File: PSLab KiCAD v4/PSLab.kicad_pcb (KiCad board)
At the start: 4 copper layers, 101.6 x 53.3 mm, 142 parts, among them CON1 USB-MICRO-B, J1 Programmer, J12 Sensors, J2 SQRs, J3 LA, J4 OSC_Pins, J5 Sin, J6 I2C, J7 IDs, J8 TX_RX_ES, J9 Test_Vs, P1 Power_Sources, P7 NRF, Q1 MMBT3906, Q2 MMBT3904, Q3 MMBT3906, U1 MCP2200, U10 TL082, U11 6S21, U12 6S21, U13 TL082, U15 ESP8266, U16 TL082, U2 74HC126, U3 PIC24EP256GP204, U4 TC1240A, U5 7660, U6 LM1117-3.3, U7 LM324, U8 TL082, U9 MCP4728, X1 12MHz

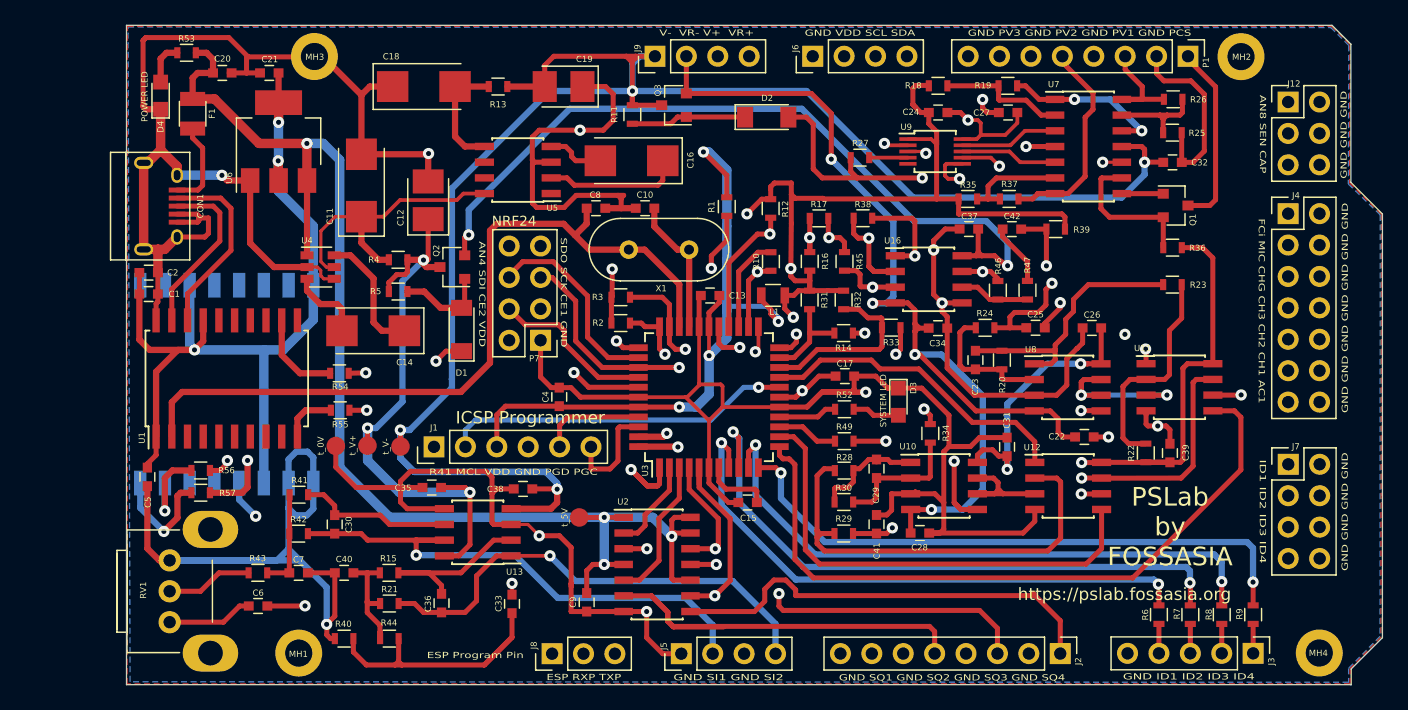
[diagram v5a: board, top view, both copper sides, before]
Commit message: Added guard rings for OSC
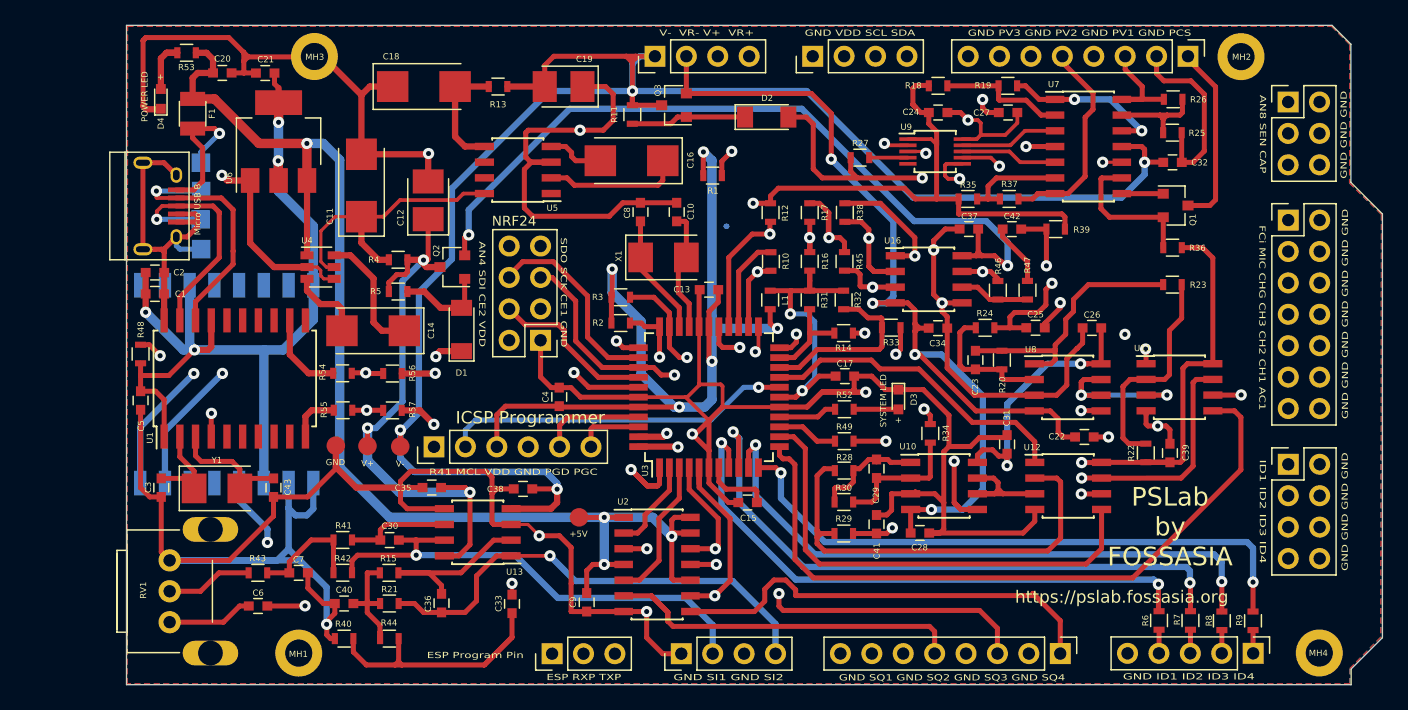
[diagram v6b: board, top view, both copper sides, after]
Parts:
- removed t_0V, t_5V, t_V+, t_V-: TEST, Measurement_Points:Measurement_Point_Round-SMD-Pad_Small
- added C3: 22p, Capacitors_SMD:C_0603, F.Cu at (93.8, 97.6)
- added C43: 22p, Capacitors_SMD:C_0603, F.Cu at (102.8, 97.6)
- added J10: GND, Measurement_Points:Measurement_Point_Square-SMD-Pad_Small, B.Cu at (97.0, 78.3)
- added J11: Vbus, Measurement_Points:Measurement_Point_Square-SMD-Pad_Small, B.Cu at (97.0, 71.4)
- added J13: D+, Measurement_Points:Measurement_Point_Square-SMD-Pad_Small, B.Cu at (97.0, 75.9)
- added J14: D-, Measurement_Points:Measurement_Point_Square-SMD-Pad_Small, B.Cu at (97.0, 73.7)
- added R48: 4.7k, Resistors_SMD:R_0603, F.Cu at (92.1, 86.8)
- added TP1: TEST, Measurement_Points:Measurement_Point_Round-SMD-Pad_Small, F.Cu at (113.1, 94.3)
- added TP2: TEST, Measurement_Points:Measurement_Point_Round-SMD-Pad_Small, F.Cu at (110.4, 94.3)
- added TP3: TEST, Measurement_Points:Measurement_Point_Round-SMD-Pad_Small, F.Cu at (127.5, 100.0)
- added TP4: TEST, Measurement_Points:Measurement_Point_Round-SMD-Pad_Small, F.Cu at (107.9, 94.2)
- added Y1: 12MHz, Crystals:Crystal_SMD_5032-2pin_5.0x3.2mm, F.Cu at (98.3, 97.7)
- CON1: value USB-MICRO-B -> USB-MINI-B
- D3, D4: footprint LEDs:LED_0805 -> LEDs:LED_0603
- L1: footprint Inductors_SMD:L_0805 -> Inductors_SMD:L_0603
- X1: value 12MHz -> 8MHz; footprint Crystals:Crystal_HC49-U_Vertical -> Crystals:Crystal_SMD_5032-2pin_5.0x3.2mm
- moved R56 17.4 mm to (112.5, 88.4), turned to 180 degrees
- moved R57 16.9 mm to (112.5, 91.4), turned to 180 degrees
- moved C5 6.20 mm to (92.1, 90.6)
- moved R41 5.10 mm to (108.4, 101.9)
- moved R42 4.77 mm to (108.4, 104.5)
- moved C30 4.62 mm to (112.2, 101.9), turned to 180 degrees
- moved C8 3.61 mm to (132.5, 75.3), turned to 270 degrees
- moved X1 2.88 mm to (134.4, 79.0)
- moved R1 2.76 mm to (138.3, 72.4), turned to 0 degrees
- moved C10 2.58 mm to (135.4, 75.3), turned to 270 degrees
- moved C40 2.48 mm to (108.5, 107.0)
- moved R38 1.53 mm to (149.1, 75.4), turned to 90 degrees
- moved R17 0.89 mm to (146.2, 75.4), turned to 90 degrees
- moved U1 0.65 mm to (99.7, 88.8)
- moved J4 0.52 mm to (184.9, 76.0)
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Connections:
- C8 pad 2: 12MHz -> Net-(C8-Pad2)
- U1 pad 2: 12MHz -> OS1
- U1 pad 3: (no net) -> OS2
- U1 pad 4: (no net) -> Net-(R48-Pad2)
- U3 pad 31: 12MHz -> Net-(C8-Pad2)
- X1 pad 1: 12MHz -> Net-(C8-Pad2)
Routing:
- net 12MHz: track 68.6 -> 0.00 mm
- net /RxD: track 153.9 -> 94.4 mm, vias 3 -> 2
- net /TxD: track 124.1 -> 73.6 mm, vias 3 -> 2
- net V-: track 193.7 -> 157.3 mm
- net Vdd: track 238.4 -> 210.2 mm, vias 8 -> 9
- net /ETxD: track 12.0 -> 34.8 mm, vias 1 -> 2
- net /ERxD: track 10.4 -> 32.1 mm, vias 1 -> 2
- net AVdd: track 175.8 -> 154.7 mm, vias 6 -> 5
- net SINE1: track 68.5 -> 48.7 mm
- net +5V: track 123.3 -> 105.2 mm
- net SDO: track 83.7 -> 100.2 mm
- net VR-: track 102.9 -> 87.8 mm
- net /SQR2: track 45.4 -> 31.2 mm
- net GND: track 804.0 -> 815.7 mm, vias 15 -> 16
- net Net-(R48-Pad2): track 0.00 -> 10.2 mm, vias 0 -> 2
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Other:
- rule via_min_size: 0.5 -> 0.3
- board text added: "+"
- board text added: "+5V"
- board text added: "4th Rev @ 29 Jan 18"
- board text added: "D+"
- board text added: "D-"
- board text added: "GND"
- board text added: "Micro USB B"
- board text added: "V+"
- board text added: "V-"
- board text added: "Vbus"
- board text removed: "4th Rev @ 23 Jan 17"

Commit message: Grounded mount holes
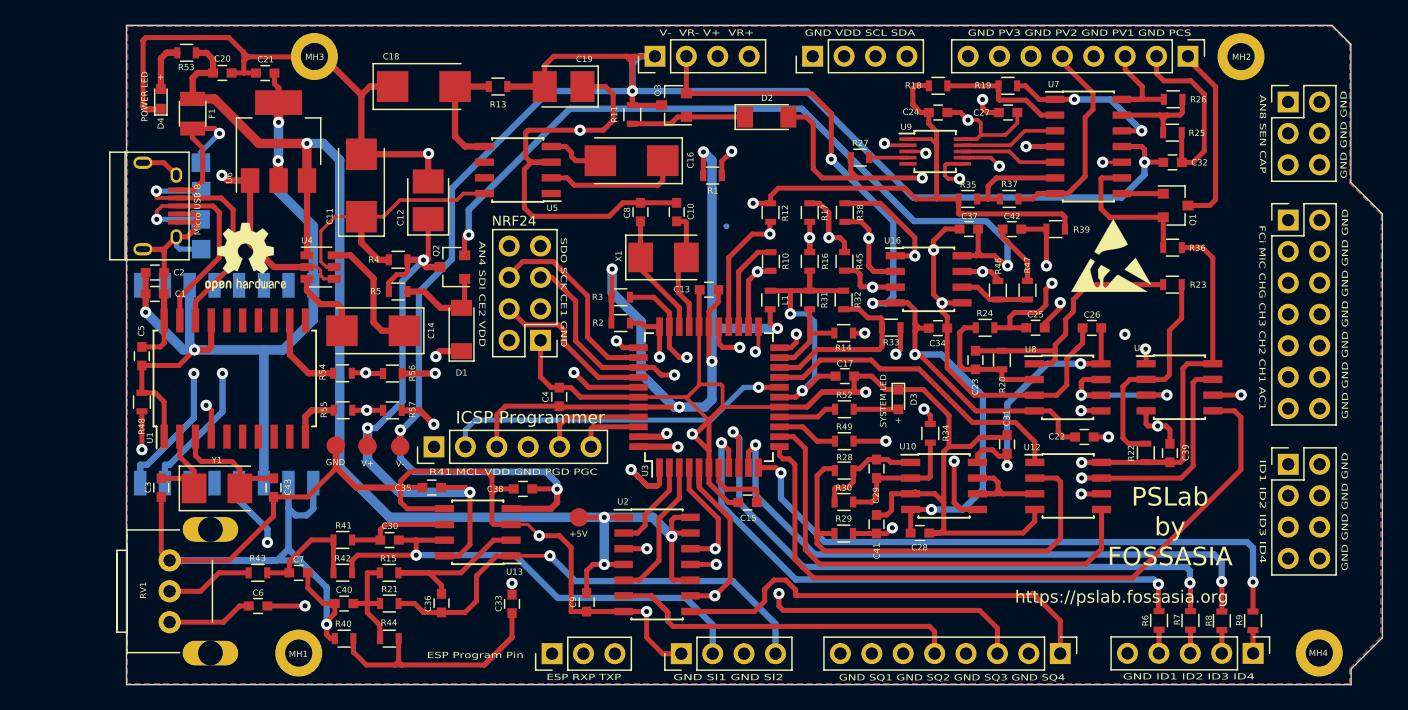
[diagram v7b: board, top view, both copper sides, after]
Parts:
- added REF***: OSHW-Logo2_7.3x6mm_SilkScreen, Symbols:OSHW-Logo2_7.3x6mm_SilkScreen, F.Cu at (100.6, 79.0)
- added REF***: ESD-Logo_6.6x6mm_SilkScreen, Symbols:ESD-Logo_6.6x6mm_SilkScreen, F.Cu at (170.6, 78.8)
- moved R48 3.89 mm to (92.2, 90.7), turned to 270 degrees
- moved C5 3.58 mm to (92.2, 87.0), turned to 90 degrees
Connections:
- MH1 pad 1: (no net) -> GND
- MH4 pad 1: (no net) -> GND
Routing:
- net GND: track 815.7 -> 832.8 mm
- net Net-(R48-Pad2): track 10.2 -> 12.5 mm
- net /ETxD: track 34.8 -> 36.1 mm
- net Vdd: track 210.2 -> 209.5 mm

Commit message: Gerber files updated
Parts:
- moved REF*** 0.39 mm to (170.7, 79.2)
- moved REF*** 0.11 mm to (100.7, 79.0)
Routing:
- net GND: track 832.8 -> 851.2 mm
- net V-: track 157.3 -> 168.2 mm
- net AN4: track 42.9 -> 38.7 mm
- net Vdd: track 209.5 -> 211.8 mm
- net VR+: track 125.8 -> 123.5 mm
- net AN8: track 63.3 -> 61.6 mm
- net V+: track 133.4 -> 134.8 mm
- net /ETxD: track 36.1 -> 37.2 mm
- net /SEN: track 57.1 -> 56.1 mm
- net /ERxD: track 32.3 -> 33.3 mm
- net /CAP: track 53.0 -> 52.4 mm
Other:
- board size 101.6 x 53.3 mm -> 99 x 53.3 mm
